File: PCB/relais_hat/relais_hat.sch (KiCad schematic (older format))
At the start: 55 parts, among them IC1 UCC27324D, IC2 UCC27324D, J1 Conn_01x03, J10 Conn_01x02, J11 Conn_01x02, J12 Conn_01x03, J13 DB9_Female, J14 Conn_01x02, J15 Conn_01x02, J16 Conn_01x02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

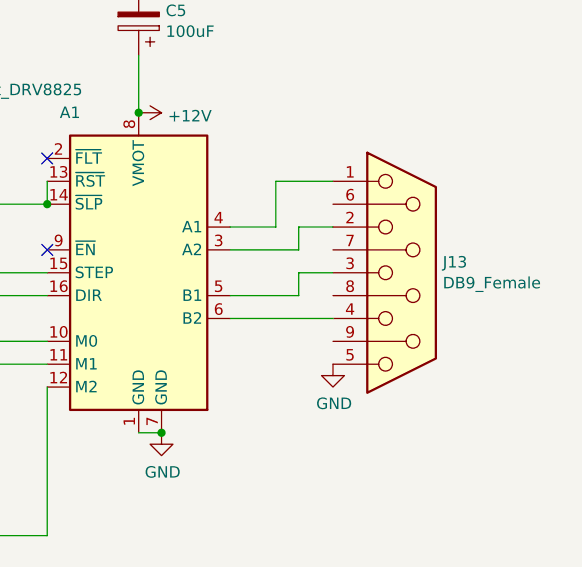
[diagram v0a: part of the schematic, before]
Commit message: add temp 1-wire in db9 connector
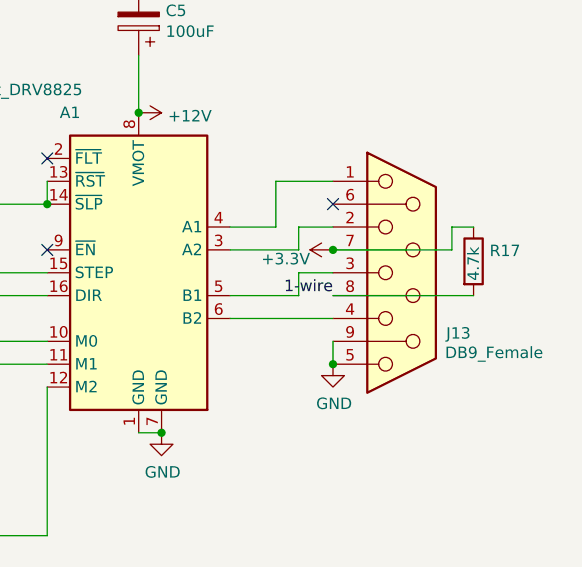
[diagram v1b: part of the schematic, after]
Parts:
- added R17: 4.7k, Resistor_SMD:R_0805_2012Metric, symbol Device:R
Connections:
- net +3V3: now also J13.7, R17.1
- net 1-wire: now also J13.8, R17.2
- net GND: now also J13.9
- no-connect marks 20 -> 21
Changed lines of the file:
@@
 U 1 1 5E90F5B2
 P 10100 4950
-F 0 "J13" H 10280 4996 50  0000 L CNN
-F 1 "DB9_Female" H 10280 4905 50  0000 L CNN
+F 0 "J13" H 10295 4685 50  0000 L CNN
+F 1 "DB9_Female" H 10290 4600 50  0000 L CNN
 F 2 "Connector_Dsub:DSUB-9_Female_Horizontal_P2.77x2.84mm_EdgePinOffset4.94mm_Housed_MountingHolesOffset7.48mm" H 10100 4950 50  0001 C CNN
 F 3 " ~" H 10100 4950 50  0001 C CNN
@@
 	0    -1   -1   0
 $EndComp
+Wire Wire Line
+	9800 5250 9800 5350
+Connection ~ 9800 5350
+$Comp
+L power:+3.3V #PWR0138
+U 1 1 5FEA8693
+P 9800 4850
+F 0 "#PWR0138" H 9800 4700 50  0001 C CNN
+F 1 "+3.3V" V 9760 4950 50  0000 L CNN
+F 2 "" H 9800 4850 50  0001 C CNN
+F 3 "" H 9800 4850 50  0001 C CNN
+	1    9800 4850
+	0    -1   -1   0
+$EndComp
+Text Label 9800 5050 2    50   ~ 0
+1-wire
+NoConn ~ 9800 4650
+$Comp
+L Device:R R17
+U 1 1 5FEBBB73
+P 10415 4900
+F 0 "R17" H 10485 4946 50  0000 L CNN
+F 1 "4.7k" V 10415 4815 50  0000 L CNN
+F 2 "Resistor_SMD:R_0805_2012Metric" V 10345 4900 50  0001 C CNN
+F 3 "~" H 10415 4900 50  0001 C CNN
+F 4 "C17673" H 10415 4900 50  0001 C CNN "LCSC"
+	1    10415 4900
+	1    0    0    -1
+$EndComp
+Wire Wire Line
+	9800 5050 10415 5050
+Wire Wire Line
+	9800 4850 10320 4850
+Wire Wire Line
+	10320 4850 10320 4750
+Wire Wire Line
+	10320 4750 10415 4750
+Connection ~ 9800 4850
 $EndSCHEMATC

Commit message: add R 10k on source/gate
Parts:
- added R18, R19, R20, R21: 10k, Resistor_SMD:R_0805_2012Metric, symbol Device:R
- renumbered Q3 to Q1, Q4 to Q2, Q1 to Q3, Q2 to Q4
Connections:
- net at J16.2 (Pin_2), J6.2 (Pin_2), J9.2 (Pin_2)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: now also R19.2
- net at J15.2 (Pin_2), J4.2 (Pin_2), J8.2 (Pin_2)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: now also R21.2
- net at J10.2 (Pin_2), J18.2 (Pin_2), J7.2 (Pin_2)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: now also R18.2
- net at J11.2 (Pin_2), J17.2 (Pin_2), J5.2 (Pin_2)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: now also R20.2
- net at Q1.1 (G), R15.1: now also R21.1
- net at Q2.1 (G), R16.1: now also R20.1
- net at Q3.1 (G), R9.1: now also R19.1
- net at Q4.1 (G), R10.1: now also R18.1
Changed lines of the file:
@@
 P 6360 3640
 F 0 "J5" V 6460 3690 50  0000 L CNN
-F 1 "Screw_Terminal_01x02" V 6175 2640 50  0000 L CNN
+F 1 "Screw_Terminal_01x02" H 6090 3865 50  0000 L CNN
 F 2 "TerminalBlock:TerminalBlock_bornier-2_P5.08mm" H 6360 3640 50  0001 C CNN
 F 3 "~" H 6360 3640 50  0001 C CNN
@@
 P 5265 3585
 AR Path="/5FE91F35/5FEB420F" Ref="Q?"  Part="1"
-AR Path="/5FEB420F" Ref="Q4"  Part="1"
-F 0 "Q4" H 5665 3850 50  0000 C CNN
+AR Path="/5FEB420F" Ref="Q2"  Part="1"
+F 0 "Q2" H 5665 3850 50  0000 C CNN
 F 1 "FDD8447L-F085" H 5665 3759 50  0000 C CNN
 F 2 "FDD8447L:FDD8447LF085" H 5915 3685 50  0001 L CNN
@@
 P 3100 5825
 AR Path="/5FE91F35/5FEC0563" Ref="Q?"  Part="1"
-AR Path="/5FEC0563" Ref="Q1"  Part="1"
-F 0 "Q1" H 3500 6090 50  0000 C CNN
+AR Path="/5FEC0563" Ref="Q3"  Part="1"
+F 0 "Q3" H 3500 6090 50  0000 C CNN
 F 1 "FDD8447L-F085" H 3500 5999 50  0000 C CNN
 F 2 "FDD8447L:FDD8447LF085" H 3750 5925 50  0001 L CNN
@@
 P 3100 6625
 AR Path="/5FE91F35/5FEC0570" Ref="Q?"  Part="1"
-AR Path="/5FEC0570" Ref="Q2"  Part="1"
-F 0 "Q2" H 3500 6890 50  0000 C CNN
+AR Path="/5FEC0570" Ref="Q4"  Part="1"
+F 0 "Q4" H 3500 6890 50  0000 C CNN
 F 1 "FDD8447L-F085" H 3500 6799 50  0000 C CNN
 F 2 "FDD8447L:FDD8447LF085" H 3750 6725 50  0001 L CNN
@@
 P 5265 2785
 AR Path="/5FE91F35/5FEB4202" Ref="Q?"  Part="1"
-AR Path="/5FEB4202" Ref="Q3"  Part="1"
-F 0 "Q3" H 5665 3050 50  0000 C CNN
+AR Path="/5FEB4202" Ref="Q1"  Part="1"
+F 0 "Q1" H 5665 3050 50  0000 C CNN
 F 1 "FDD8447L-F085" H 5665 2959 50  0000 C CNN
 F 2 "FDD8447L:FDD8447LF085" H 5915 2885 50  0001 L CNN
@@
 	3100 5925 3100 6070
 Wire Wire Line
-	3100 6070 3900 6070
-Wire Wire Line
 	5265 3805 6070 3805
 Wire Wire Line
@@
 Connection ~ 4005 5880
 Wire Wire Line
-	4005 5980 3900 5980
+	4005 5980 3960 5980
 Wire Wire Line
 	3900 5980 3900 6070
@@
 P 5565 3135
 F 0 "#PWR0134" H 5565 2885 50  0001 C CNN
-F 1 "GND" V 5570 3007 50  0000 R CNN
+F 1 "GND" V 5490 3055 50  0000 R CNN
 F 2 "" H 5565 3135 50  0001 C CNN
 F 3 "" H 5565 3135 50  0001 C CNN
@@
 P 5820 3955
 F 0 "#PWR0135" H 5820 3705 50  0001 C CNN
-F 1 "GND" V 5825 3827 50  0000 R CNN
+F 1 "GND" V 5690 3930 50  0000 R CNN
 F 2 "" H 5820 3955 50  0001 C CNN
 F 3 "" H 5820 3955 50  0001 C CNN
@@
 P 3710 7070
 F 0 "#PWR0137" H 3710 6820 50  0001 C CNN
-F 1 "GND" V 3715 6942 50  0000 R CNN
+F 1 "GND" V 3534 7061 50  0000 R CNN
 F 2 "" H 3710 7070 50  0001 C CNN
 F 3 "" H 3710 7070 50  0001 C CNN
@@
 	10320 4750 10415 4750
 Connection ~ 9800 4850
+$Comp
+L Device:R R?
+U 1 1 6085B00C
+P 3975 6175
+AR Path="/5FE91F35/6085B00C" Ref="R?"  Part="1"
+AR Path="/6085B00C" Ref="R19"  Part="1"
+F 0 "R19" H 3856 6244 50  0000 C CNN
+F 1 "10k" V 3982 6164 50  0000 C CNN
+F 2 "Resistor_SMD:R_0805_2012Metric" V 3905 6175 50  0001 C CNN
+F 3 "~" H 3975 6175 50  0001 C CNN
+F 4 "C17414" V 3975 6175 50  0001 C CNN "LCSC"
+	1    3975 6175
+	0    -1   -1   0
+$EndComp
+$Comp
+L Device:R R?
+U 1 1 6086250A
+P 3941 6968
+AR Path="/5FE91F35/6086250A" Ref="R?"  Part="1"
+AR Path="/6086250A" Ref="R18"  Part="1"
+F 0 "R18" V 3838 6960 50  0000 C CNN
+F 1 "10k" V 3948 6957 50  0000 C CNN
+F 2 "Resistor_SMD:R_0805_2012Metric" V 3871 6968 50  0001 C CNN
+F 3 "~" H 3941 6968 50  0001 C CNN
+F 4 "C17414" V 3941 6968 50  0001 C CNN "LCSC"
+	1    3941 6968
+	0    -1   -1   0
+$EndComp
+Wire Wire Line
+	3995 6815 3995 6895
+Wire Wire Line
+	3995 6895 4091 6895
+Wire Wire Line
+	4091 6895 4091 6968
+Wire Wire Line
+	3791 6968 3066 6968
+Wire Wire Line
+	3066 6968 3066 6708
+Wire Wire Line
+	3066 6708 3100 6708
+Wire Wire Line
+	3100 6708 3100 6625
+Connection ~ 3100 6625
+Wire Wire Line
+	3100 5825 3100 5900
+Wire Wire Line
+	3100 5900 3050 5900
+Wire Wire Line
+	3050 5900 3050 6125
+Wire Wire Line
+	3050 6125 3825 6125
+Wire Wire Line
+	3825 6125 3825 6175
+Connection ~ 3100 5825
+Wire Wire Line
+	3100 6070 3900 6070
+Wire Wire Line
+	3960 5980 3960 6080
+Wire Wire Line
+	3960 6080 4125 6080
+Wire Wire Line
+	4125 6080 4125 6175
+Connection ~ 3960 5980
+Wire Wire Line
+	3960 5980 3900 5980
+$Comp
+L Device:R R?
+U 1 1 608FCFFF
+P 6090 3090
+AR Path="/5FE91F35/608FCFFF" Ref="R?"  Part="1"
+AR Path="/608FCFFF" Ref="R21"  Part="1"
+F 0 "R21" V 5985 3040 50  0000 C CNN
+F 1 "10k" V 6097 3079 50  0000 C CNN
+F 2 "Resistor_SMD:R_0805_2012Metric" V 6020 3090 50  0001 C CNN
+F 3 "~" H 6090 3090 50  0001 C CNN
+F 4 "C17414" V 6090 3090 50  0001 C CNN "LCSC"
+	1    6090 3090
+	0    -1   -1   0
+$EndComp
+$Comp
+L Device:R R?
+U 1 1 609053C4
+P 6080 3895
+AR Path="/5FE91F35/609053C4" Ref="R?"  Part="1"
+AR Path="/609053C4" Ref="R20"  Part="1"
+F 0 "R20" V 5975 3870 50  0000 C CNN
+F 1 "10k" V 6087 3884 50  0000 C CNN
+F 2 "Resistor_SMD:R_0805_2012Metric" V 6010 3895 50  0001 C CNN
+F 3 "~" H 6080 3895 50  0001 C CNN
+F 4 "C17414" V 6080 3895 50  0001 C CNN "LCSC"
+	1    6080 3895
+	0    -1   -1   0
+$EndComp
+Wire Wire Line
+	6215 2945 6215 3035
+Wire Wire Line
+	6215 3035 6240 3035
+Wire Wire Line
+	6240 3035 6240 3090
+Wire Wire Line
+	5940 3090 5245 3090
+Wire Wire Line
+	5245 3090 5245 2825
+Wire Wire Line
+	5245 2825 5265 2825
+Wire Wire Line
+	5265 2825 5265 2785
+Connection ~ 5265 2785
+Wire Wire Line
+	6160 3740 6160 3810
+Wire Wire Line
+	6160 3810 6230 3810
+Wire Wire Line
+	6230 3810 6230 3895
+Wire Wire Line
+	5930 3895 5240 3895
+Wire Wire Line
+	5240 3895 5240 3645
+Wire Wire Line
+	5240 3645 5265 3645
+Wire Wire Line
+	5265 3645 5265 3585
+Connection ~ 5265 3585
 $EndSCHEMATC
